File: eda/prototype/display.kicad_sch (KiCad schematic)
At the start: 4 parts, among them J2 Conn_01x16, U14 74HCT541, U15 74HCT541, U16 74HCT541

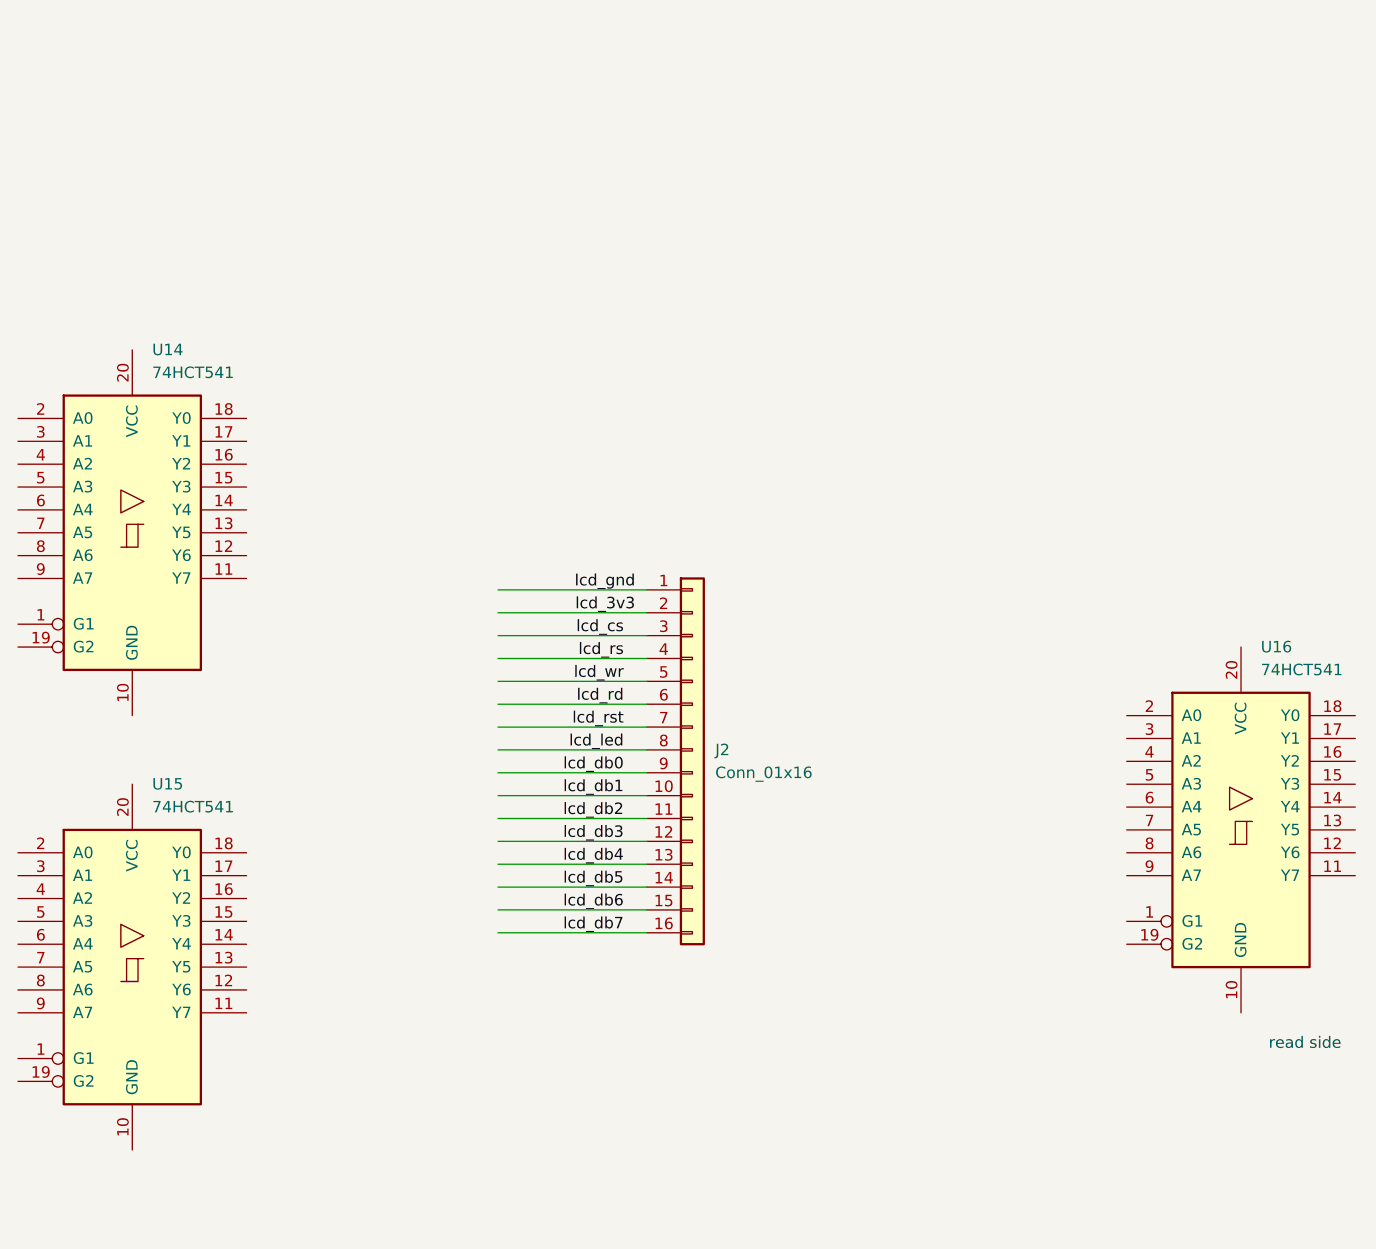
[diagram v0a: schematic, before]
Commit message: eda: prototype: sync schematic
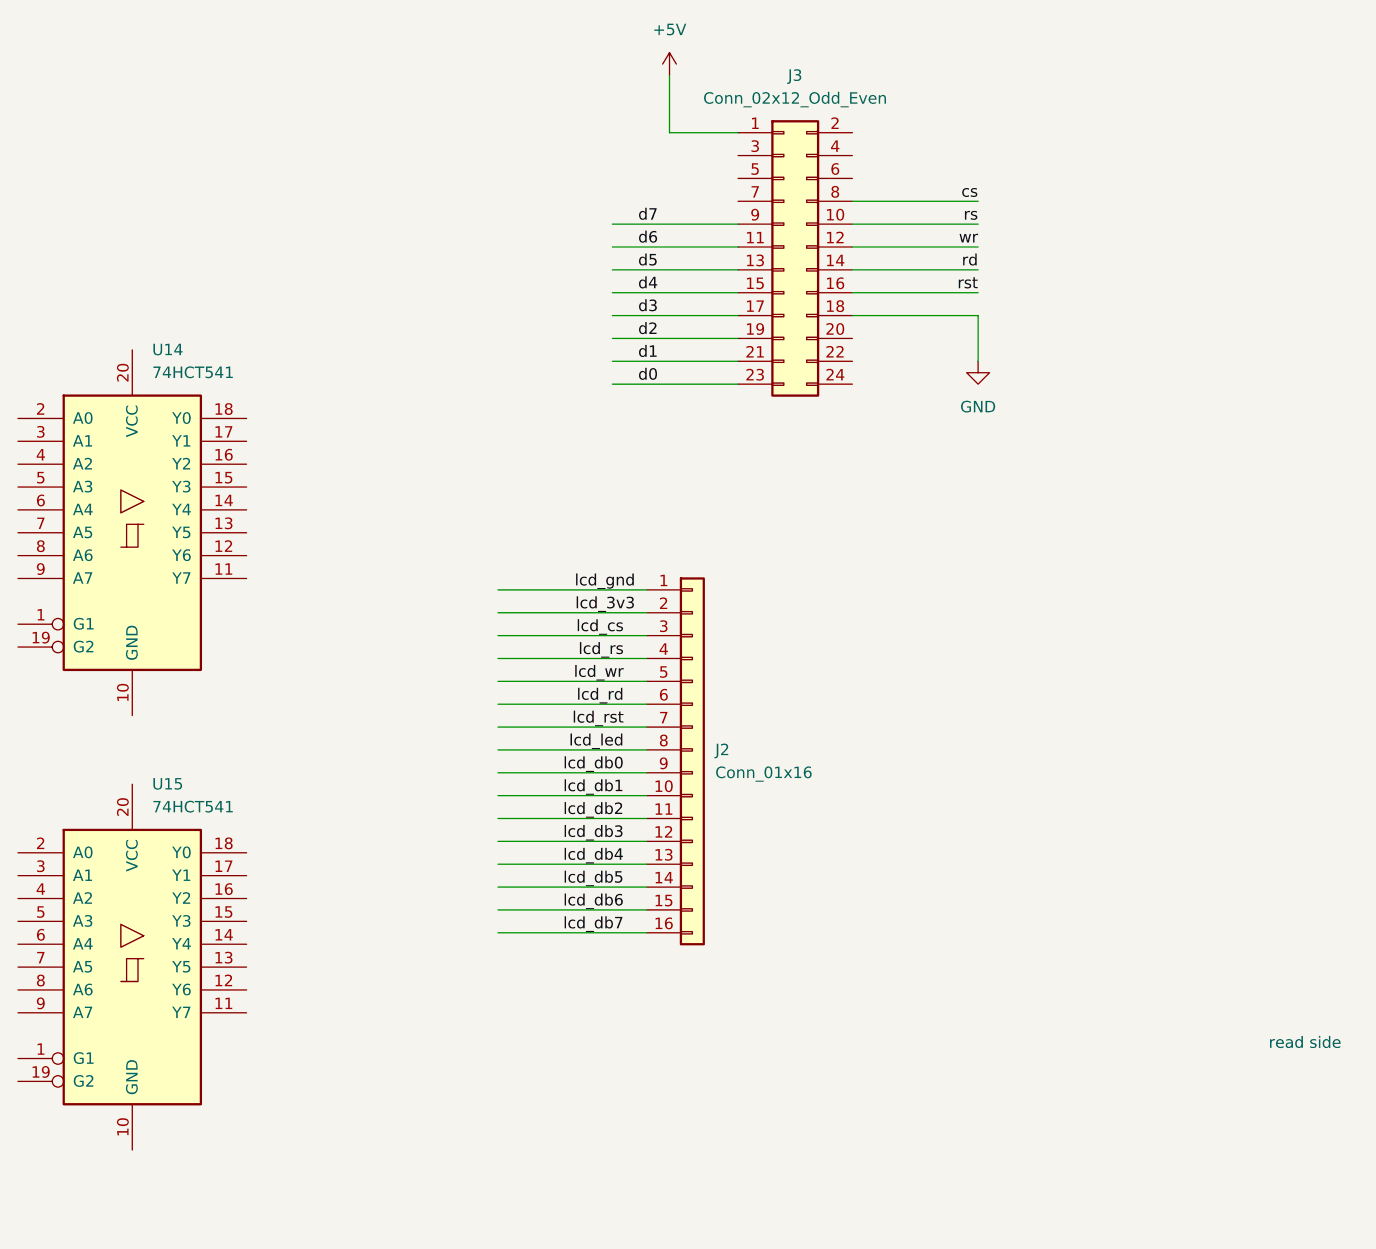
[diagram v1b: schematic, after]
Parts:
- removed U16: 74HCT541, symbol 74xx:74HCT541
- added J3: Conn_02x12_Odd_Even, symbol Connector_Generic:Conn_02x12_Odd_Even
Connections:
- new net +5V: J3.1 (Pin_1)
- new net GND: J3.18 (Pin_18)
- new net cs: J3.8 (Pin_8)
- new net d0: J3.23 (Pin_23)
- new net d1: J3.21 (Pin_21)
- new net d2: J3.19 (Pin_19)
- new net d3: J3.17 (Pin_17)
- new net d4: J3.15 (Pin_15)
- new net d5: J3.13 (Pin_13)
- new net d6: J3.11 (Pin_11)
- new net d7: J3.9 (Pin_9)
- new net rd: J3.14 (Pin_14)
- new net rs: J3.10 (Pin_10)
- new net rst: J3.16 (Pin_16)
- new net wr: J3.12 (Pin_12)

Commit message: eda:prototype: jankorama rng
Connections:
- net GND: now also U14.10 (GND), U15.10 (GND)
- net +3.3V: now reaches U15.20 (VCC)
- net +3.3V: now also U14.20 (VCC)
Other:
- moved on the sheet: U14
